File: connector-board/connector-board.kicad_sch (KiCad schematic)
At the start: 13 parts, among them J1 Conn_01x15_Pin, J10 Conn_01x03_Socket, J2 Conn_01x02_Socket, J3 Conn_01x02_Socket, J4 Conn_01x04_Socket, J5 Conn_01x03_Socket, J6 Conn_01x02_Socket, J7 Conn_01x03_Socket, J8 Conn_01x03_Socket, J9 Conn_01x03_Socket

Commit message: feat: split hardware into Main Board and Connector Board projects
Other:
- title: Watering System Daughterboard -> Connector Board
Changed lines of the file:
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@@
 	(paper "A4")
 	(title_block
-		(title "Watering System Daughterboard")
+		(title "Connector Board")
 		(rev "See GitHub")
 		(comment 3 "into smaller cables for individual plants")
@@
 		)
 		(instances
-			(project "connector_board"
+			(project "connector-board"
 				(path "/97006c64-4d9a-49c1-90c8-c7dde4458483"
 					(reference "#PWR017")
@@
 		)
 		(instances
-			(project "connector_board"
+			(project "connector-board"
 				(path "/97006c64-4d9a-49c1-90c8-c7dde4458483"
 					(reference "#PWR022")
@@
 		)
 		(instances
-			(project "connector_board"
+			(project "connector-board"
 				(path "/97006c64-4d9a-49c1-90c8-c7dde4458483"
 					(reference "#PWR015")
@@
 		)
 		(instances
-			(project "connector_board"
+			(project "connector-board"
 				(path "/97006c64-4d9a-49c1-90c8-c7dde4458483"
 					(reference "#PWR020")
@@
 		)
 		(instances
-			(project "connector_board"
+			(project "connector-board"
 				(path "/97006c64-4d9a-49c1-90c8-c7dde4458483"
 					(reference "#PWR019")
@@
 		)
 		(instances
-			(project "connector_board"
+			(project "connector-board"
 				(path "/97006c64-4d9a-49c1-90c8-c7dde4458483"
 					(reference "#PWR09")
@@
 		)
 		(instances
-			(project "connector_board"
+			(project "connector-board"
 				(path "/97006c64-4d9a-49c1-90c8-c7dde4458483"
 					(reference "J10")
@@
 		)
 		(instances
-			(project "connector_board"
+			(project "connector-board"
 				(path "/97006c64-4d9a-49c1-90c8-c7dde4458483"
 					(reference "J6")
@@
 		)
 		(instances
-			(project "connector_board"
+			(project "connector-board"
 				(path "/97006c64-4d9a-49c1-90c8-c7dde4458483"
 					(reference "#PWR01")
@@
 		)
 		(instances
-			(project "connector_board"
+			(project "connector-board"
 				(path "/97006c64-4d9a-49c1-90c8-c7dde4458483"
 					(reference "#PWR011")
@@
 		)
 		(instances
-			(project "connector_board"
+			(project "connector-board"
 				(path "/97006c64-4d9a-49c1-90c8-c7dde4458483"
 					(reference "#PWR012")
@@
 		)
 		(instances
-			(project "connector_board"
+			(project "connector-board"
 				(path "/97006c64-4d9a-49c1-90c8-c7dde4458483"
 					(reference "#PWR04")
@@
 		)
 		(instances
-			(project "connector_board"
+			(project "connector-board"
 				(path "/97006c64-4d9a-49c1-90c8-c7dde4458483"
 					(reference "#PWR02")
@@
 		)
 		(instances
-			(project "connector_board"
+			(project "connector-board"
 				(path "/97006c64-4d9a-49c1-90c8-c7dde4458483"
 					(reference "#PWR07")
@@
 		)
 		(instances
-			(project "connector_board"
+			(project "connector-board"
 				(path "/97006c64-4d9a-49c1-90c8-c7dde4458483"
 					(reference "#PWR03")
@@
 		)
 		(instances
-			(project "connector_board"
+			(project "connector-board"
 				(path "/97006c64-4d9a-49c1-90c8-c7dde4458483"
 					(reference "#PWR010")
@@
 		)
 		(instances
-			(project "connector_board"
+			(project "connector-board"
 				(path "/97006c64-4d9a-49c1-90c8-c7dde4458483"
 					(reference "J5")
@@
 		)
 		(instances
-			(project "connector_board"
+			(project "connector-board"
 				(path "/97006c64-4d9a-49c1-90c8-c7dde4458483"
 					(reference "#PWR021")
@@
 		)
 		(instances
-			(project "connector_board"
+			(project "connector-board"
 				(path "/97006c64-4d9a-49c1-90c8-c7dde4458483"
 					(reference "#PWR013")
@@
 		)
 		(instances
-			(project "connector_board"
+			(project "connector-board"
 				(path "/97006c64-4d9a-49c1-90c8-c7dde4458483"
 					(reference "J2")
@@
 		)
 		(instances
-			(project "connector_board"
+			(project "connector-board"
 				(path "/97006c64-4d9a-49c1-90c8-c7dde4458483"
 					(reference "J7")
@@
 		)
 		(instances
-			(project "connector_board"
+			(project "connector-board"
 				(path "/97006c64-4d9a-49c1-90c8-c7dde4458483"
 					(reference "R1")
@@
 		)
 		(instances
-			(project "connector_board"
+			(project "connector-board"
 				(path "/97006c64-4d9a-49c1-90c8-c7dde4458483"
 					(reference "J8")
@@
 		)
 		(instances
-			(project "connector_board"
+			(project "connector-board"
 				(path "/97006c64-4d9a-49c1-90c8-c7dde4458483"
 					(reference "#PWR06")
@@
 		)
 		(instances
-			(project "connector_board"
+			(project "connector-board"
 				(path "/97006c64-4d9a-49c1-90c8-c7dde4458483"
 					(reference "#PWR05")
@@
 		)
 		(instances
-			(project "connector_board"
+			(project "connector-board"
 				(path "/97006c64-4d9a-49c1-90c8-c7dde4458483"
 					(reference "J4")
@@
 		)
 		(instances
-			(project "connector_board"
+			(project "connector-board"
 				(path "/97006c64-4d9a-49c1-90c8-c7dde4458483"
 					(reference "J1")
@@
 		)
 		(instances
-			(project "connector_board"
+			(project "connector-board"
 				(path "/97006c64-4d9a-49c1-90c8-c7dde4458483"
 					(reference "C1")
@@
 		)
 		(instances
-			(project "connector_board"
+			(project "connector-board"
 				(path "/97006c64-4d9a-49c1-90c8-c7dde4458483"
 					(reference "C2")
@@
 		)
 		(instances
-			(project "connector_board"
+			(project "connector-board"
 				(path "/97006c64-4d9a-49c1-90c8-c7dde4458483"
 					(reference "#PWR08")
@@
 		)
 		(instances
-			(project "connector_board"
+			(project "connector-board"
 				(path "/97006c64-4d9a-49c1-90c8-c7dde4458483"
 					(reference "J3")
@@
 		)
 		(instances
-			(project "connector_board"
+			(project "connector-board"
 				(path "/97006c64-4d9a-49c1-90c8-c7dde4458483"
 					(reference "#PWR018")
@@
 		)
 		(instances
-			(project "connector_board"
+			(project "connector-board"
 				(path "/97006c64-4d9a-49c1-90c8-c7dde4458483"
 					(reference "#PWR014")
@@
 		)
 		(instances
-			(project "connector_board"
+			(project "connector-board"
 				(path "/97006c64-4d9a-49c1-90c8-c7dde4458483"
 					(reference "J9")
@@
 		)
 		(instances
-			(project "connector_board"
+			(project "connector-board"
 				(path "/97006c64-4d9a-49c1-90c8-c7dde4458483"
 					(reference "#PWR016")

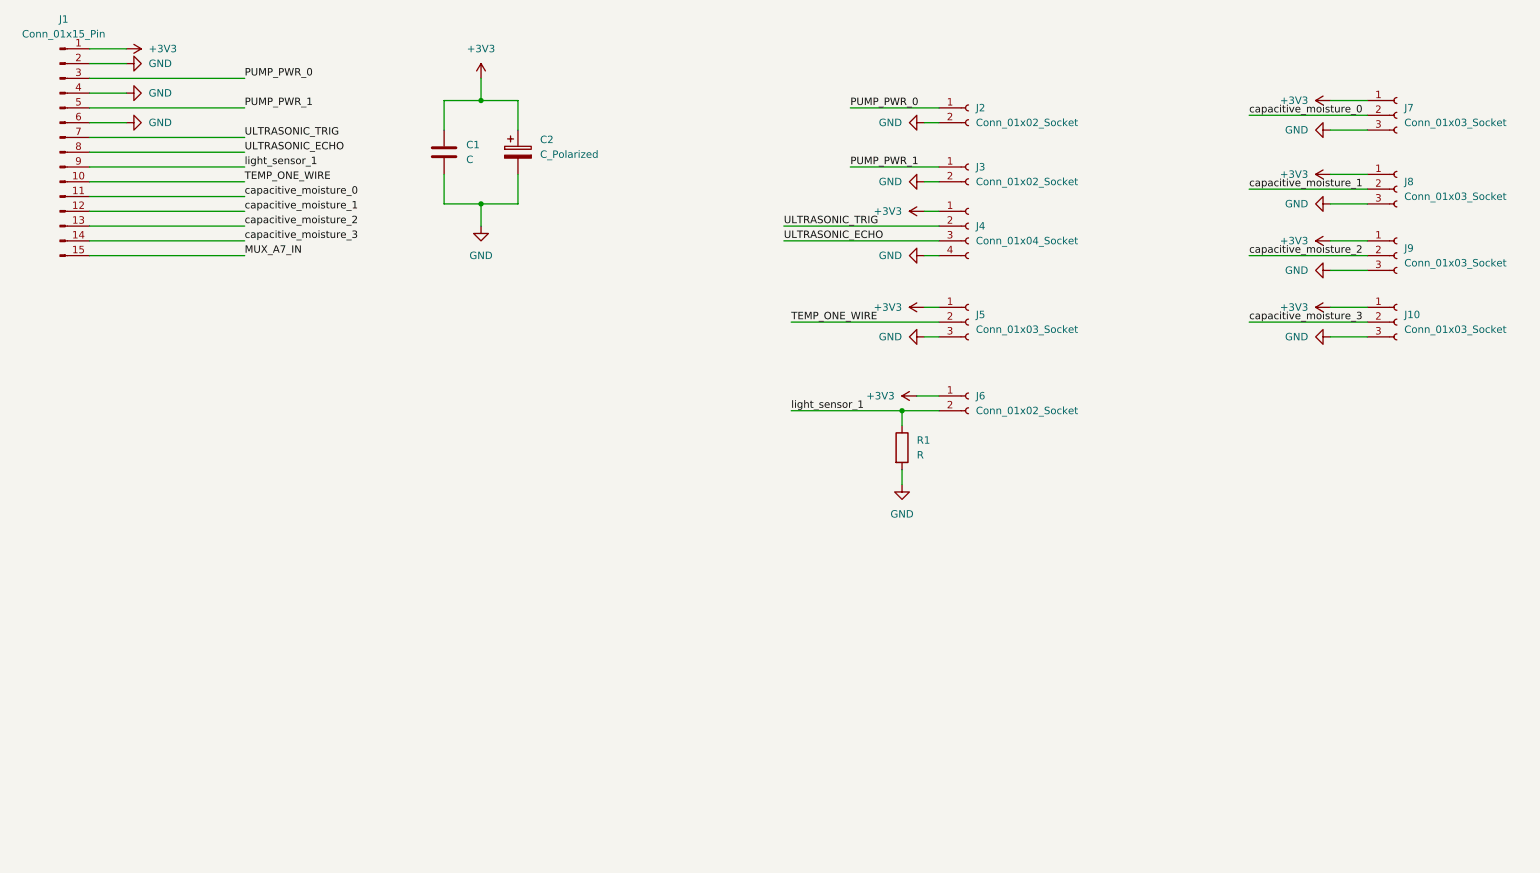
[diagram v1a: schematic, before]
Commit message: style(connector-board): group and space schematic connections
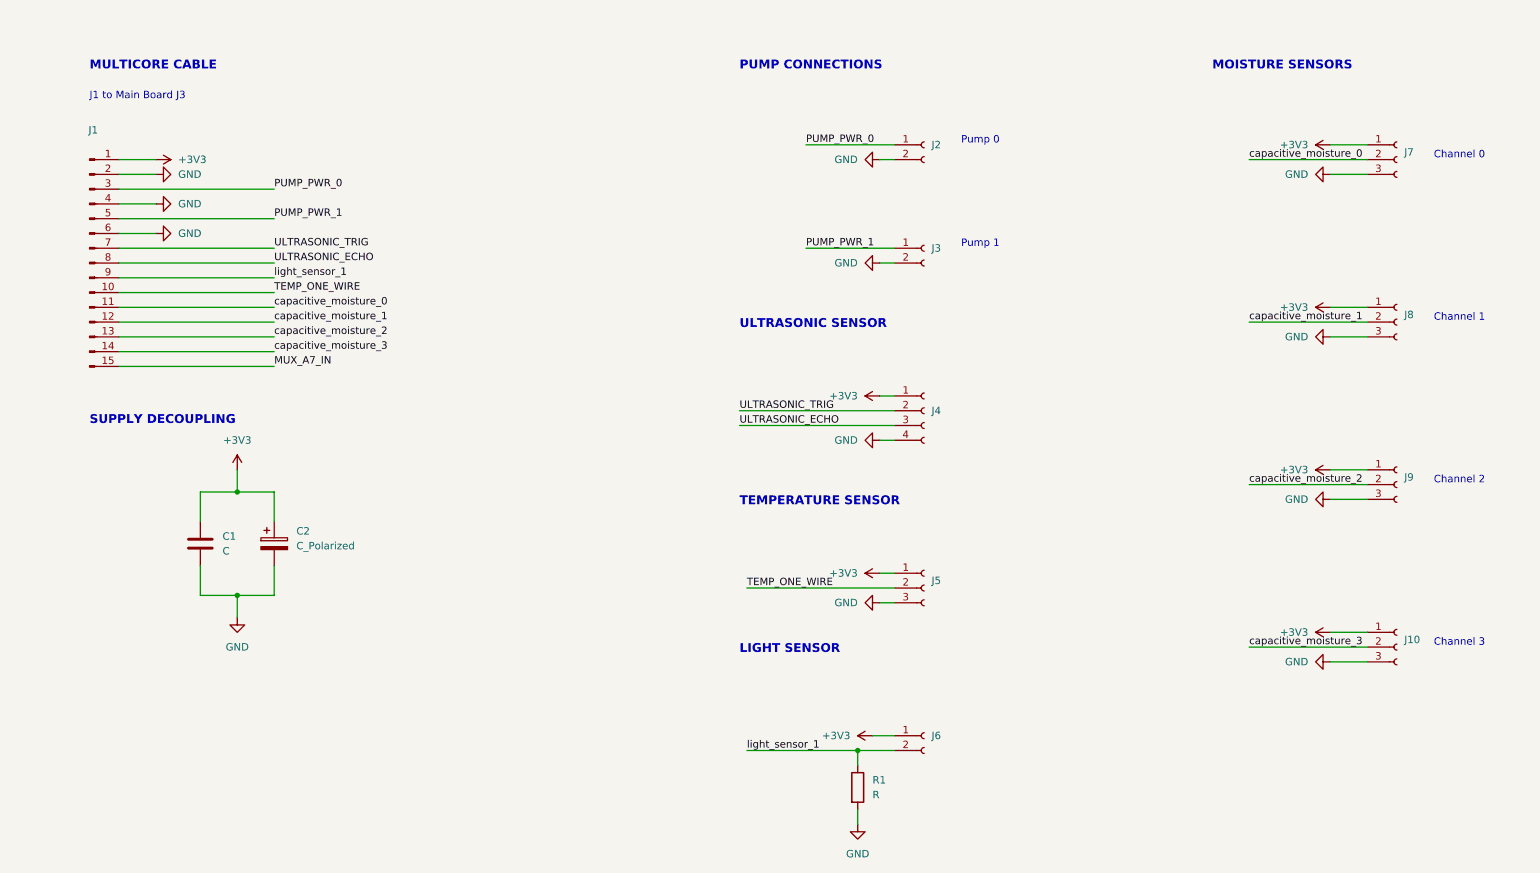
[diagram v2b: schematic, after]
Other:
- note added: "Channel 0"
- note added: "Channel 1"
- note added: "Channel 2"
- note added: "Channel 3"
- note added: "J1 to Main Board J3"
- note added: "LIGHT SENSOR"
- note added: "MOISTURE SENSORS"
- note added: "MULTICORE CABLE"
- note added: "PUMP CONNECTIONS"
- note added: "Pump 0"
- note added: "Pump 1"
- note added: "SUPPLY DECOUPLING"
- note added: "TEMPERATURE SENSOR"
- note added: "ULTRASONIC SENSOR"
- moved on the sheet: C1, C2, J1, J10, J2, J3, J4, J5, J6, J7, J8, J9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

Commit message: fix(connector-board): declare external power and unused cable pin
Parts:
- C1: value C -> 100nF
- C2: value C_Polarized -> 100uF
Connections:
- net MUX_A7_IN: no longer names the net of J1.15 (Pin_15)
- no-connect marks 0 -> 1
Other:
- note added: "MUX_A7_IN - spare"
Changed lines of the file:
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@@
 		(effects (font (size 1.27 1.27)) (justify left bottom))
 	)
+	(no_connect (at 30.48 76.2))
+	(text "MUX_A7_IN - spare" (at 35.56 76.2 0) (effects (font (size 1.27 1.27)) (justify left bottom)))
+	(wire (pts (xy 57.15 97.79) (xy 73.66 97.79)) (stroke (width 0) (type default)))
+	(junction (at 57.15 97.79) (diameter 0) (color 0 0 0 0))
+	(wire (pts (xy 57.15 115.57) (xy 73.66 115.57)) (stroke (width 0) (type default)))
+	(junction (at 57.15 115.57) (diameter 0) (color 0 0 0 0))
 	(junction
 		(at 157.4800 142.2400)
@@
 	(wire
 		(pts
-			(xy 30.4800 76.2000) (xy 57.1500 76.2000)
-		)
-		(stroke
-			(width 0)
-			(type default)
-		)
-	)
-	(wire
-		(pts
 			(xy 148.5900 55.8800) (xy 163.8300 55.8800)
 		)
@@
 		)
 	)
-	(label "MUX_A7_IN"
-		(at 57.1500 76.2000 0)
-		(effects
-			(font
-				(size 1.27 1.27)
-			)
-			(justify left bottom)
-		)
-	)
 	(label "ULTRASONIC_ECHO"
 		(at 57.1500 58.4200 0)
@@
 			)
 		)
-		(property "Value" "C"
+		(property "Value" "100nF"
 			(at 48.2600 107.9499 0)
 			(show_name no)
@@
 			)
 		)
-		(property "Value" "C_Polarized"
+		(property "Value" "100uF"
 			(at 60.9600 107.0609 0)
 			(show_name no)
@@
 					(unit 1)
 				)
+			)
+		)
+	)
+	(symbol (lib_id "power:PWR_FLAG") (at 73.66 97.79 0) (unit 1)
+		(body_style 1) (exclude_from_sim no) (in_bom yes) (on_board yes) (in_pos_files yes) (dnp no)
+		(property "Reference" "#FLG01"
+			(hide yes)
+			(at 73.66 99.695 0)
+			(show_name no)
+			(do_not_autoplace no)
+			(effects
+				(font
+					(size 1.27 1.27)
+				)
+			)
+		)
+		(property "Value" "PWR_FLAG"
+			(at 73.66 93.98 0)
+			(show_name no)
+			(do_not_autoplace no)
+			(effects
+				(font
+					(size 1.27 1.27)
+				)
+			)
+		)
+		(property "Footprint" ""
+			(at 73.66 97.79 0)
+			(hide yes)
+			(show_name no)
+			(do_not_autoplace no)
+			(effects
+				(font
+					(size 1.27 1.27)
+				)
+			)
+		)
+		(property "Datasheet" ""
+			(at 73.66 97.79 0)
+			(hide yes)
+			(show_name no)
+			(do_not_autoplace no)
+			(effects
+				(font
+					(size 1.27 1.27)
+				)
+			)
+		)
+		(property "Description" "Special symbol for telling ERC where power comes from"
+			(at 73.66 97.79 0)
+			(hide yes)
+			(show_name no)
+			(do_not_autoplace no)
+			(effects
+				(font
+					(size 1.27 1.27)
+				)
+			)
+		)
+		(pin "1")
+		(instances
+			(project "connector-board"
+				(path "/97006c64-4d9a-49c1-90c8-c7dde4458483"
+					(reference "#FLG01")
+					(unit 1)
+				)
+			)
+		)
+	)
+	(symbol (lib_id "power:PWR_FLAG") (at 73.66 115.57 0) (unit 1)
+		(body_style 1) (exclude_from_sim no) (in_bom yes) (on_board yes) (in_pos_files yes) (dnp no)
+		(property "Reference" "#FLG02"
+			(hide yes)
+			(at 73.66 117.475 0)
+			(show_name no)
+			(do_not_autoplace no)
+			(effects
+				(font
+					(size 1.27 1.27)
+				)
+			)
+		)
+		(property "Value" "PWR_FLAG"
+			(at 73.66 111.76 0)
+			(show_name no)
+			(do_not_autoplace no)
+			(effects
+				(font
+					(size 1.27 1.27)
+				)
+			)
+		)
+		(property "Footprint" ""
+			(at 73.66 115.57 0)
+			(hide yes)
+			(show_name no)
+			(do_not_autoplace no)
+			(effects
+				(font
+					(size 1.27 1.27)
+				)
+			)
+		)
+		(property "Datasheet" ""
+			(at 73.66 115.57 0)
+			(hide yes)
+			(show_name no)
+			(do_not_autoplace no)
+			(effects
+				(font
+					(size 1.27 1.27)
+				)
+			)
+		)
+		(property "Description" "Special symbol for telling ERC where power comes from"
+			(at 73.66 115.57 0)
+			(hide yes)
+			(show_name no)
+			(do_not_autoplace no)
+			(effects
+				(font
+					(size 1.27 1.27)
+				)
+			)
+		)
+		(pin "1")
+		(instances
+			(project "connector-board"
+				(path "/97006c64-4d9a-49c1-90c8-c7dde4458483"
+					(reference "#FLG02")
+					(unit 1)
+				)

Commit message: fix: set both light sensor resistors to 10k
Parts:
- R1: value R -> 10k
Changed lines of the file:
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@@
 			)
 		)
-		(property "Value" "R"
+		(property "Value" "10k"
 			(at 160.0200 149.8599 0)
 			(show_name no)
